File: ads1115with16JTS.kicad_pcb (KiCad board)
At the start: 2 copper layers, 48.3 x 71.1 mm, 54 parts, among them J1 Conn_01x02_Pin, J10 Conn_01x02_Pin, J11 Conn_01x02_Pin, J12 Conn_01x02_Pin, J13 Conn_01x02_Pin, J14 Conn_01x02_Pin, J15 Conn_01x02_Pin, J16 Conn_01x02_Pin, J17 Conn_01x04_Pin, J18 PinSocket_1x20_P2.54mm_Vertic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, J19 PinSocket_1x20_P2.54mm_Vertic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, J2 Conn_01x02_Pin, J20 Screw_Terminal_01x02, J3 Conn_01x02_Pin, J4 Conn_01x02_Pin, J5 Conn_01x02_Pin, J6 Conn_01x02_Pin, J7 Conn_01x02_Pin, J8 Conn_01x02_Pin, J9 Conn_01x02_Pin, U1 ADS1115IDGS, U2 ADS1115IDGS, U3 ADS1115IDGS, U4 ADS1115IDGS

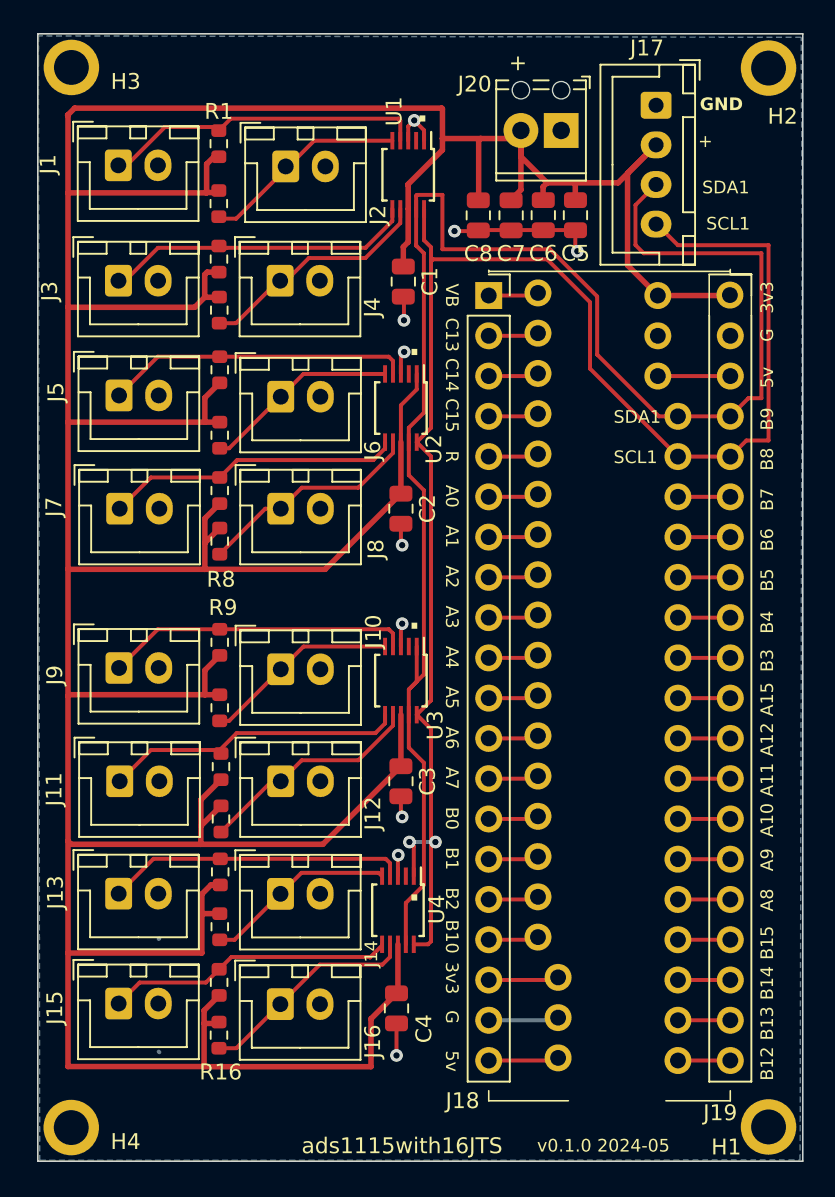
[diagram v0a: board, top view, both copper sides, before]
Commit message: added pullup on scl, sda. Other ongoing minor adjustments.
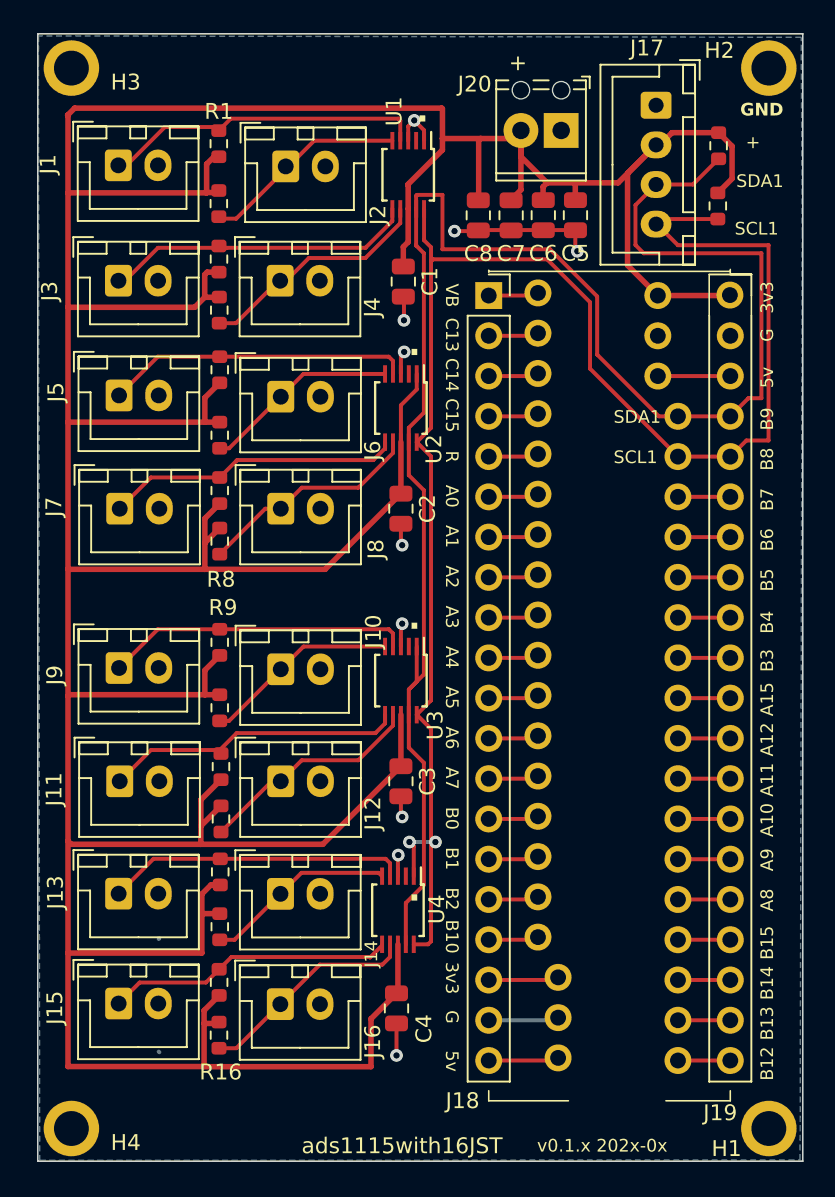
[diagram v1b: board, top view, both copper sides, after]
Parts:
- added R17: 10k, ProjectLib:R_0603_1608Metric, F.Cu at (92.4, 35.0)
- added R18: 10k, ProjectLib:R_0603_1608Metric, F.Cu at (92.5, 31.2)
- moved H1 0.10 mm to (95.7, 93.2)
- moved H4 0.06 mm to (51.6, 93.2)
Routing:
- net +3V3: track 305.5 -> 314.3 mm
- net /SDA1: track 105.3 -> 110.0 mm
- net /SCL1: track 101.8 -> 105.8 mm
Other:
- board text added: "ads1115with16JST"
- board text added: "v0.1.x 202x-0x"
- board text removed: "ads1115with16JTS"
- board text removed: "v0.1.0 2024-05"
